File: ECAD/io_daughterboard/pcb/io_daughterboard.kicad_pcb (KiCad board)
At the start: 2 copper layers, 120 x 66 mm, 90 parts, among them CON1 BARREL_JACK, J1 XF2L-0625-1A, J2 4-1734839-0, P1 CONN_02X32, P10 Slave 5B, P11 Slave 1C, P12 Slave 3C, P13 Slave 4C, P14 Slave 5C, P15 Slave 1D, P16 Slave 3D, P17 Slave 4D, P18 Slave 5D, P2 CONN_02X32, P3 Slave 1A, P4 Slave 3A, P5 Slave 4A, P6 Slave 5A, P7 Slave 1B, P8 Slave 3B, P9 Slave 4B, U1 FAN5333BSX, U10 SN74LV1T34DCKR, U11 SN74LV1T34DCKR, U2 SPX3819M5-L-3-3, U3 74HC244, U4 74HC244, U5 74HC244, U6 STMPE811QTR, U7 74HC244, U8 74HC244, U9 74HC244

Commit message: Removed all traces.
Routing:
- net GND: track 614.9 -> 0.00 mm, vias 1 -> 0
- net +3V3: track 428.1 -> 0.00 mm, vias 2 -> 0
- net +5V: track 281.8 -> 0.00 mm
- net /PC8: track 173.0 -> 0.00 mm, vias 2 -> 0
- net /PE3: track 141.4 -> 0.00 mm, vias 3 -> 0
- net /PC3: track 122.5 -> 0.00 mm, vias 4 -> 0
- net /PC13: track 114.9 -> 0.00 mm
- net /PC11: track 99.2 -> 0.00 mm, vias 2 -> 0
- net /PB7: track 95.9 -> 0.00 mm, vias 2 -> 0
- net /PF7: track 85.0 -> 0.00 mm, vias 4 -> 0
- net /LCD_DE: track 84.6 -> 0.00 mm, vias 1 -> 0
- net /PE2: track 82.6 -> 0.00 mm, vias 3 -> 0
- net /PE5: track 81.3 -> 0.00 mm, vias 3 -> 0
- net /PF8: track 77.8 -> 0.00 mm, vias 4 -> 0
- net /PA5: track 76.8 -> 0.00 mm, vias 2 -> 0
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
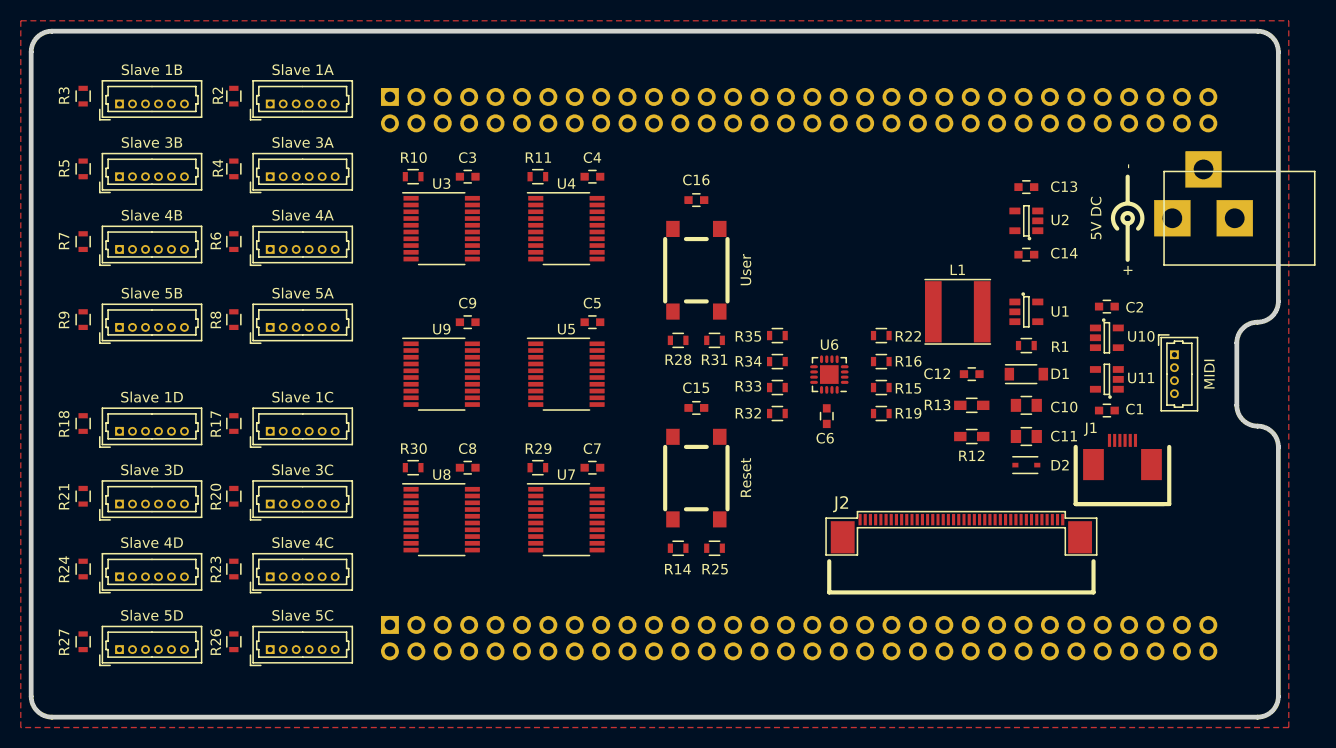
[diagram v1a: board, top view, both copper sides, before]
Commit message: Switched connectors P1 and P2.  Made traces for filter caps.
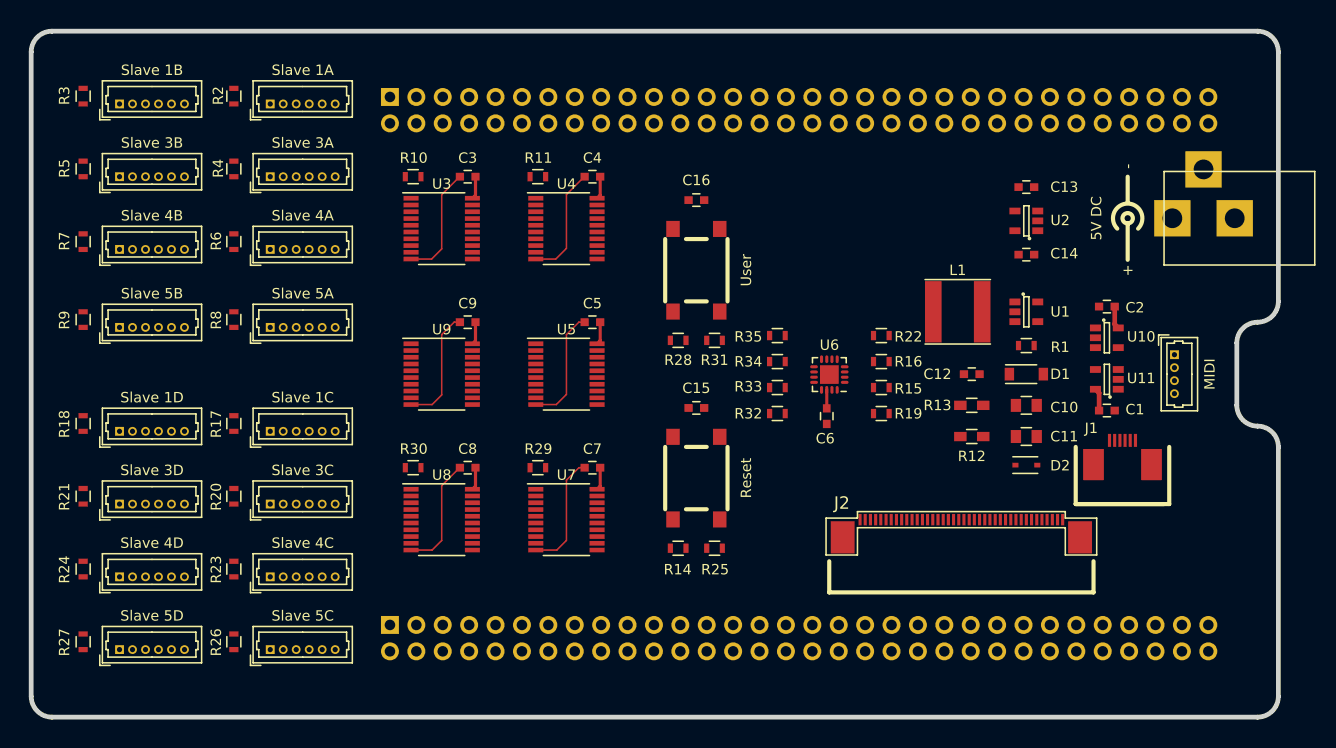
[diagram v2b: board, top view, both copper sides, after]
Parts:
- moved P1 50.8 mm to (134.5, 40.3)
- moved P2 50.8 mm to (134.5, 91.1)
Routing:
- net GND: track 0.00 -> 67.2 mm
- net +3V3: track 0.00 -> 15.0 mm
- net +5V: track 0.00 -> 4.39 mm
- removed copper zone on F.Cu, net GND
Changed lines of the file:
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@@
   (general
     (links 360)
-    (no_connects 0)
+    (no_connects 324)
     (area 84.650001 26.3 231.421429 122.700001)
     (thickness 1.6)
     (drawings 24)
-    (tracks 2051)
+    (tracks 47)
     (zones 0)
     (modules 90)
@@
   )
   (module daughterfeet:Socket_Strip_Reversed_2x32 locked (layer B.Cu)
-    (at 134.52 40.33)
+    (at 134.52 91.13)
     (descr "Through hole socket strip")
     (tags "socket strip")
@@
   )
   (module daughterfeet:Socket_Strip_Reversed_2x32 locked (layer B.Cu)
-    (at 134.52 91.13)
+    (at 134.52 40.33)
     (descr "Through hole socket strip")
     (tags "socket strip")
@@
   (gr_line (start 102 34) (end 218 34) (angle -90) (layer Edge.Cuts) (width 0.4572))
   (gr_line (start 218 100) (end 102 100) (angle -90) (layer Edge.Cuts) (width 0.4572))
-  (zone (net 2) (net_name GND) (layer F.Cu) (hatch edge 0.508)
-    (connect_pads (clearance 0.1524))
-    (min_thickness 0.254)
-    (fill yes (arc_segments 16) (thermal_gap 0.508) (thermal_bridge_width 0.508))
-    (polygon
-      (pts
-        (xy 99 33) (xy 221 33) (xy 221 101) (xy 99 101)
-      )
-    )
-  )
+  (segment (start 202.75 70.5) (end 202.75 68.8) (width 0.4572) (layer F.Cu) (net 1))
+  (segment (start 202.75 68.8) (end 202.4 68.45) (width 0.4572) (layer F.Cu) (net 1))
+  (segment (start 204.25 60.5) (end 204.25 62.2) (width 0.4572) (layer F.Cu) (net 1))
+  (segment (start 204.25 62.2) (end 204.6 62.55) (width 0.4572) (layer F.Cu) (net 1))
+  (segment (start 139.5 83) (end 138.575 83.925) (width 0.1524) (layer F.Cu) (net 2))
+  (segment (start 138.575 83.925) (end 136.55 83.925) (width 0.1524) (layer F.Cu) (net 2))
+  (segment (start 139.5 77.725) (end 139.5 83) (width 0.1524) (layer F.Cu) (net 2))
+  (segment (start 141.25 76) (end 141.225 76) (width 0.1524) (layer F.Cu) (net 2))
+  (segment (start 141.225 76) (end 139.5 77.725) (width 0.1524) (layer F.Cu) (net 2))
+  (segment (start 151.5 83) (end 150.575 83.925) (width 0.1524) (layer F.Cu) (net 2))
+  (segment (start 150.575 83.925) (end 148.55 83.925) (width 0.1524) (layer F.Cu) (net 2))
+  (segment (start 151.5 77.1976) (end 151.5 83) (width 0.1524) (layer F.Cu) (net 2))
+  (segment (start 153.25 76) (end 152.6976 76) (width 0.1524) (layer F.Cu) (net 2))
+  (segment (start 152.6976 76) (end 151.5 77.1976) (width 0.1524) (layer F.Cu) (net 2))
+  (segment (start 139.5 69) (end 138.575 69.925) (width 0.1524) (layer F.Cu) (net 2))
+  (segment (start 138.575 69.925) (end 136.55 69.925) (width 0.1524) (layer F.Cu) (net 2))
+  (segment (start 139.5 63.1976) (end 139.5 69) (width 0.1524) (layer F.Cu) (net 2))
+  (segment (start 141.25 62) (end 140.6976 62) (width 0.1524) (layer F.Cu) (net 2))
+  (segment (start 140.6976 62) (end 139.5 63.1976) (width 0.1524) (layer F.Cu) (net 2))
+  (segment (start 151.5 68.95) (end 150.525 69.925) (width 0.1524) (layer F.Cu) (net 2))
+  (segment (start 150.525 69.925) (end 148.55 69.925) (width 0.1524) (layer F.Cu) (net 2))
+  (segment (start 151.5 63.1976) (end 151.5 68.95) (width 0.1524) (layer F.Cu) (net 2))
+  (segment (start 153.25 62) (end 152.6976 62) (width 0.1524) (layer F.Cu) (net 2))
+  (segment (start 152.6976 62) (end 151.5 63.1976) (width 0.1524) (layer F.Cu) (net 2))
+  (segment (start 151.5 54.9) (end 150.475 55.925) (width 0.1524) (layer F.Cu) (net 2))
+  (segment (start 150.475 55.925) (end 148.55 55.925) (width 0.1524) (layer F.Cu) (net 2))
+  (segment (start 151.5 49.725) (end 151.5 54.9) (width 0.1524) (layer F.Cu) (net 2))
+  (segment (start 153.25 48) (end 153.225 48) (width 0.1524) (layer F.Cu) (net 2))
+  (segment (start 153.225 48) (end 151.5 49.725) (width 0.1524) (layer F.Cu) (net 2))
+  (segment (start 141.25 48) (end 141.225 48) (width 0.1524) (layer F.Cu) (net 2))
+  (segment (start 141.225 48) (end 139.5 49.725) (width 0.1524) (layer F.Cu) (net 2))
+  (segment (start 139.5 49.725) (end 139.5 54.95) (width 0.1524) (layer F.Cu) (net 2))
+  (segment (start 139.5 54.95) (end 138.525 55.925) (width 0.1524) (layer F.Cu) (net 2))
+  (segment (start 138.525 55.925) (end 136.55 55.925) (width 0.1524) (layer F.Cu) (net 2))
+  (segment (start 176.547 70.2892) (end 176.547 68.5142) (width 0.3048) (layer F.Cu) (net 3))
+  (segment (start 142.75 76) (end 142.75 77.775) (width 0.3048) (layer F.Cu) (net 3))
+  (segment (start 142.75 77.775) (end 142.45 78.075) (width 0.3048) (layer F.Cu) (net 3))
+  (segment (start 154.75 76) (end 154.75 77.775) (width 0.3048) (layer F.Cu) (net 3))
+  (segment (start 154.75 77.775) (end 154.45 78.075) (width 0.3048) (layer F.Cu) (net 3))
+  (segment (start 142.75 62) (end 142.75 63.775) (width 0.3048) (layer F.Cu) (net 3))
+  (segment (start 142.75 63.775) (end 142.45 64.075) (width 0.3048) (layer F.Cu) (net 3))
+  (segment (start 154.75 62) (end 154.75 63.775) (width 0.3048) (layer F.Cu) (net 3))
+  (segment (start 154.75 63.775) (end 154.45 64.075) (width 0.3048) (layer F.Cu) (net 3))
+  (segment (start 154.75 48) (end 154.75 49.775) (width 0.3048) (layer F.Cu) (net 3))
+  (segment (start 154.75 49.775) (end 154.45 50.075) (width 0.3048) (layer F.Cu) (net 3))
+  (segment (start 142.75 48) (end 142.75 49.775) (width 0.3048) (layer F.Cu) (net 3))
+  (segment (start 142.75 49.775) (end 142.45 50.075) (width 0.3048) (layer F.Cu) (net 3))
 )

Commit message: Re-routed board with P1/P2 corrected, added explicit ground-to-bypass traces.
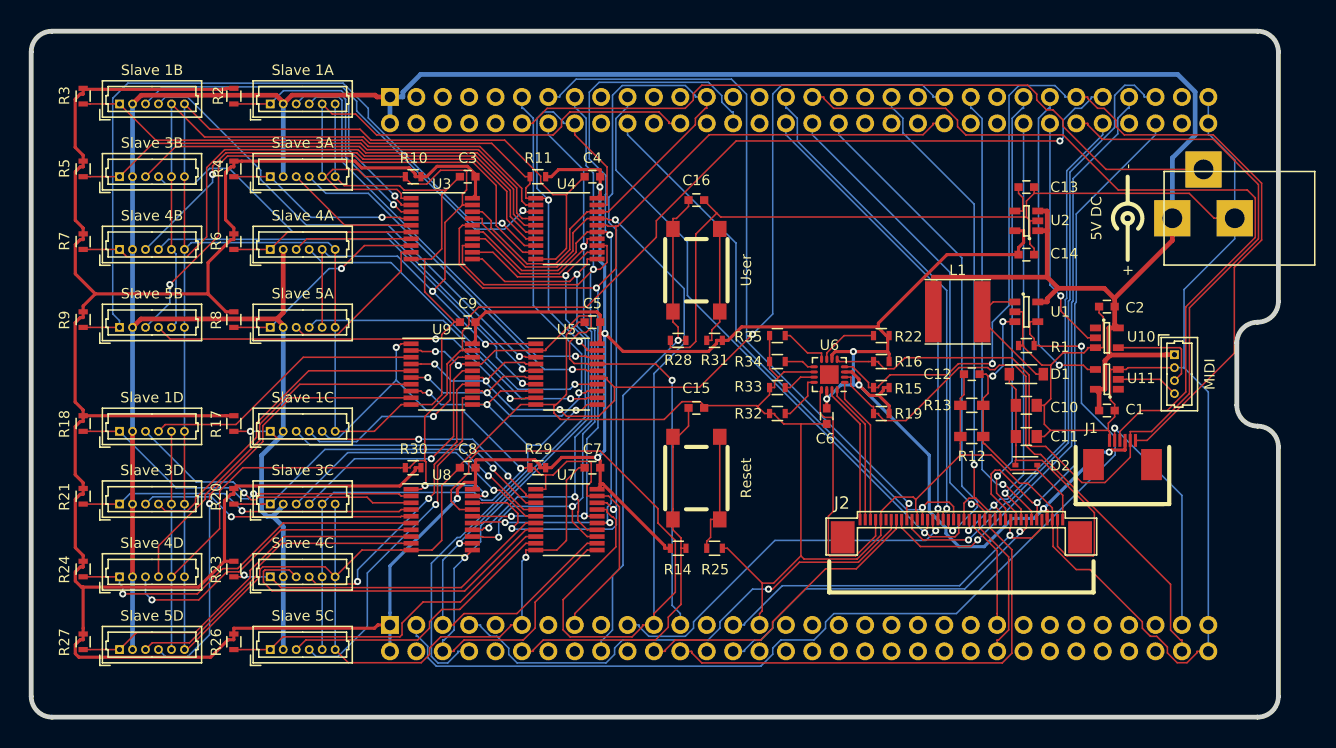
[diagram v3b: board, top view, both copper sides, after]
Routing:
- net GND: track 67.2 -> 622.1 mm, vias 0 -> 1
- net +3V3: track 15.0 -> 439.0 mm, vias 0 -> 9
- net +5V: track 4.39 -> 299.1 mm
- net /PC8: track 0.00 -> 152.0 mm, vias 0 -> 3
- net /PA5: track 0.00 -> 127.1 mm, vias 0 -> 1
- net /PB7: track 0.00 -> 115.1 mm, vias 0 -> 2
- net /PB4: track 0.00 -> 104.5 mm, vias 0 -> 2
- net /PE3: track 0.00 -> 103.6 mm, vias 0 -> 2
- net /I²C3_SCL: track 0.00 -> 102.4 mm, vias 0 -> 1
- net /LCD_PWM: track 0.00 -> 98.9 mm, vias 0 -> 1
- net /PC11: track 0.00 -> 97.9 mm, vias 0 -> 3
- net /PC3: track 0.00 -> 95.4 mm, vias 0 -> 2
- net /I²C3_SDA: track 0.00 -> 91.6 mm
- net /PB3: track 0.00 -> 90.8 mm, vias 0 -> 3
- net /PC12: track 0.00 -> 89.6 mm, vias 0 -> 4
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
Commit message: Added ground plane; widened ground traces to slave connectors.
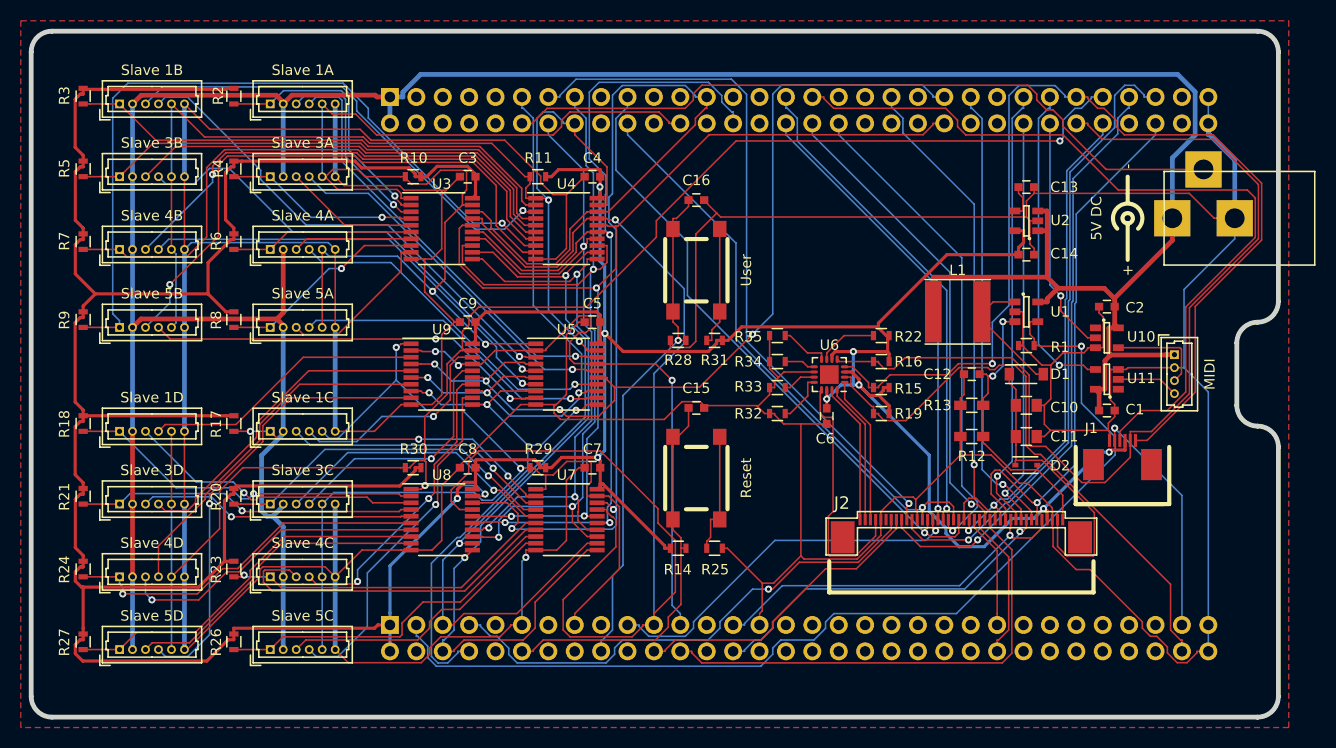
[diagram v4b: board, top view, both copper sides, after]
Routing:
- added copper zone on F.Cu, net GND

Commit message: Improved ground plane around slave connectors.
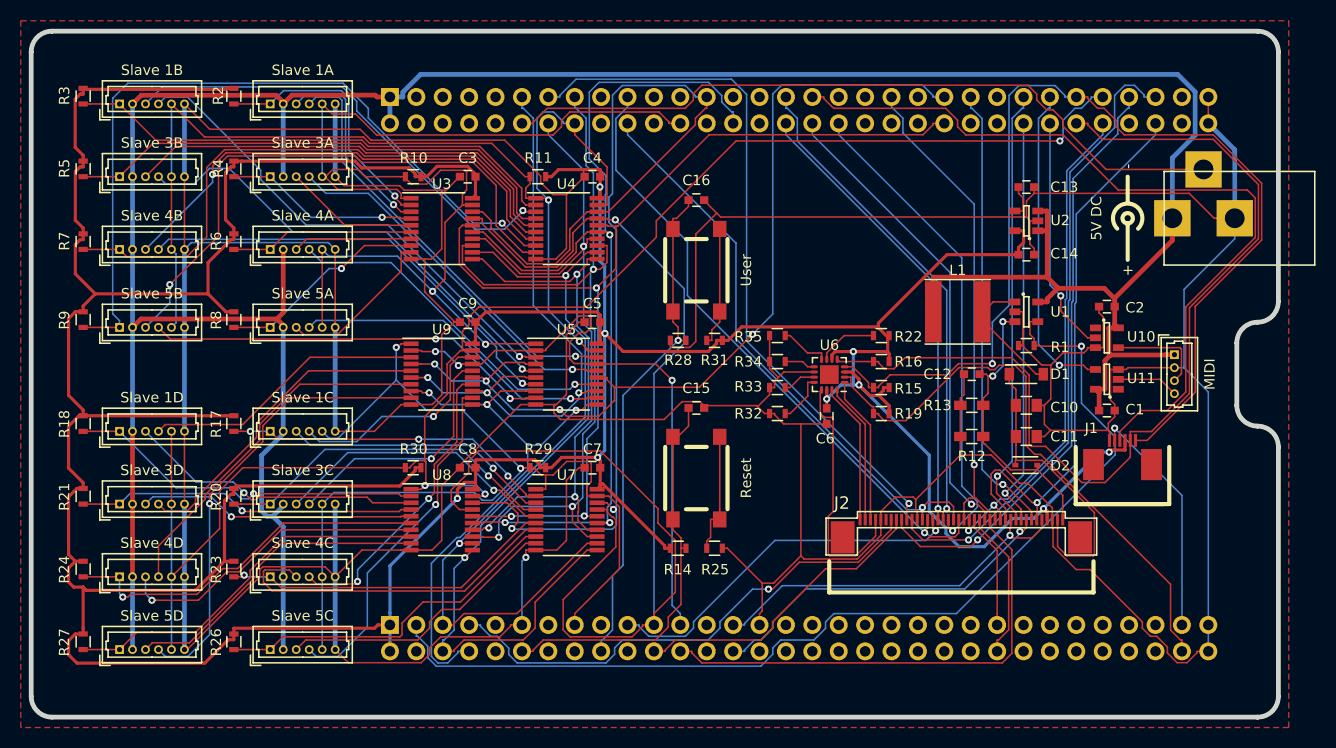
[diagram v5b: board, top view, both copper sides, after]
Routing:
- net +3V3: track 439.3 -> 444.0 mm
